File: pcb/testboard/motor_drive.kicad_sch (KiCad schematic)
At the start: 7 parts, among them IC1 TLE94112ESXUMA1, J3 Motor 1, J4 Motor 2, J5 Motor 3

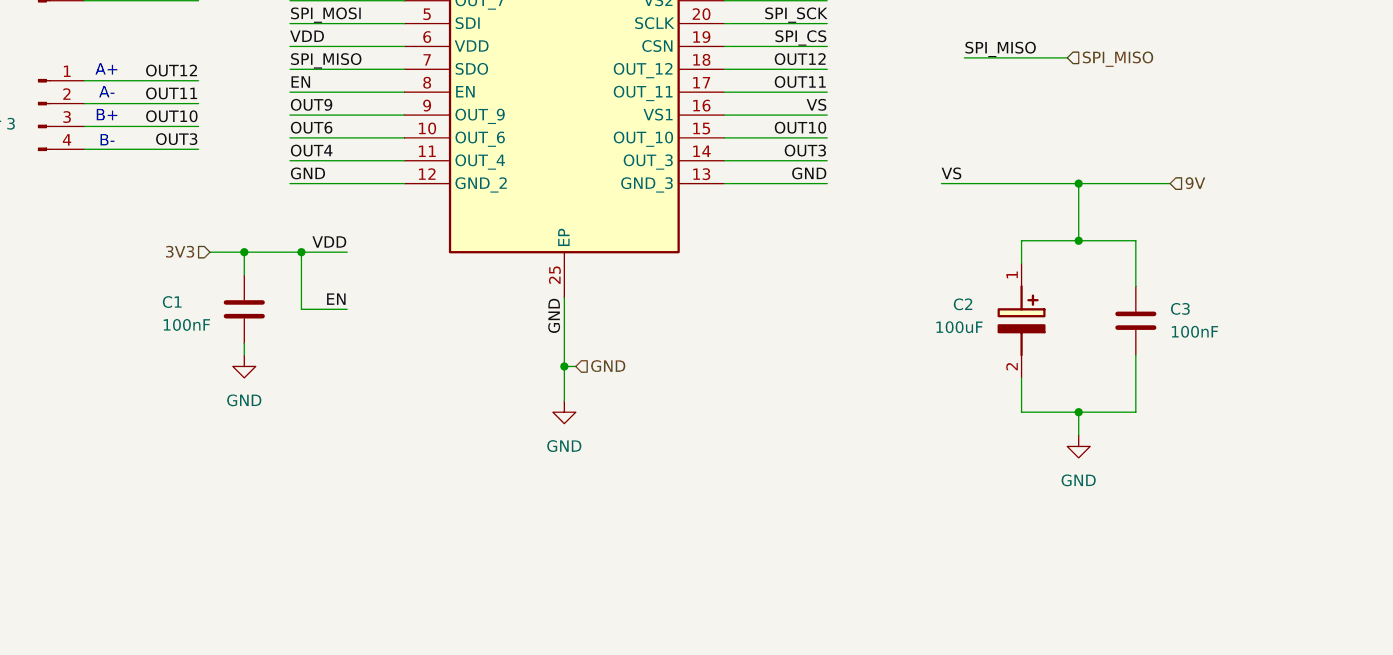
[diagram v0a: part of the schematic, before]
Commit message: Schematic final edit Added all remaining components and modifications, started PCB design
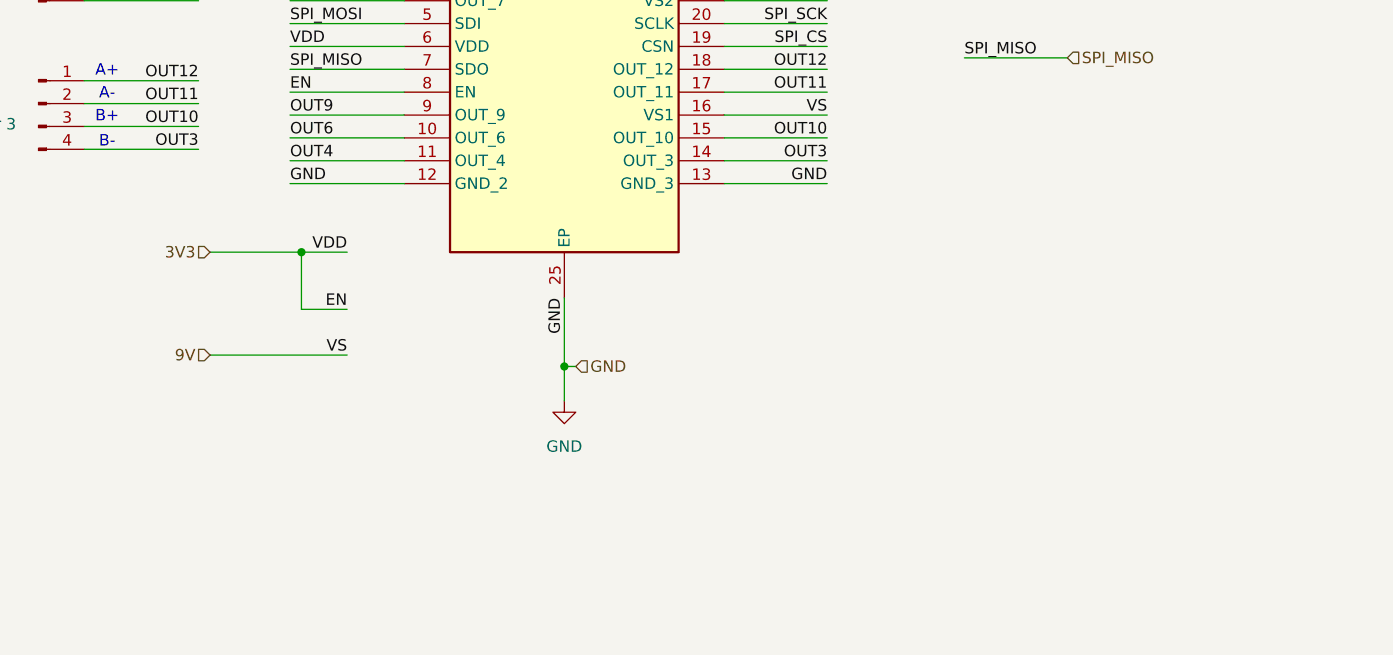
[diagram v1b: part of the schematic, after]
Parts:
- removed C1, C3: 100nF, Capacitor_SMD:C_0805_2012Metric, symbol Device:C
- removed C2: 100uF, CAPPRD250W50D655H1300, symbol EWH1EV101E11OT:EWH1EV101E11OT
- J3, J4, J5: footprint (none) -> Connector_PinSocket_1.00mm:PinSocket_1x04_P1.00mm_Vertical

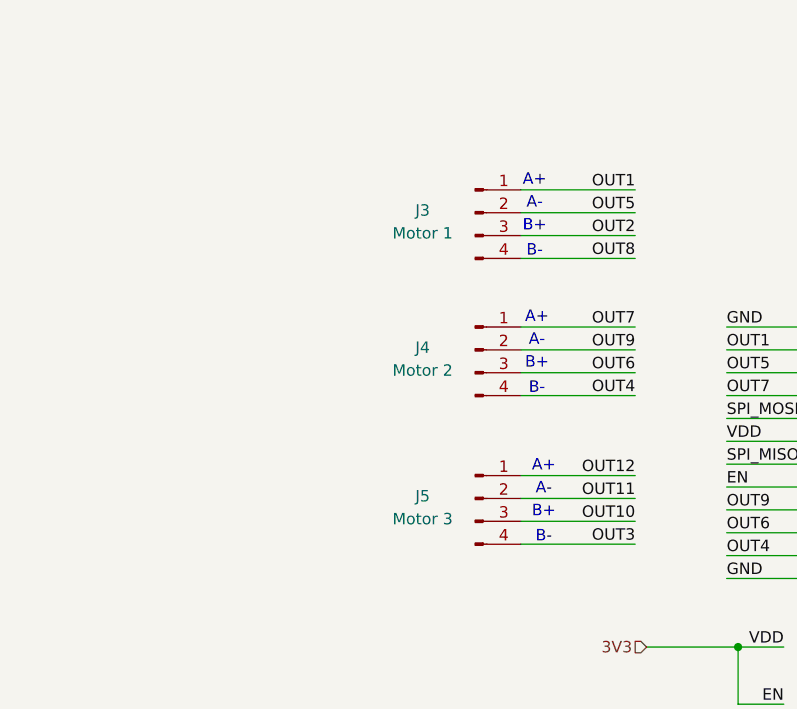
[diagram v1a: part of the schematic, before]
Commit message: routed the new connectors
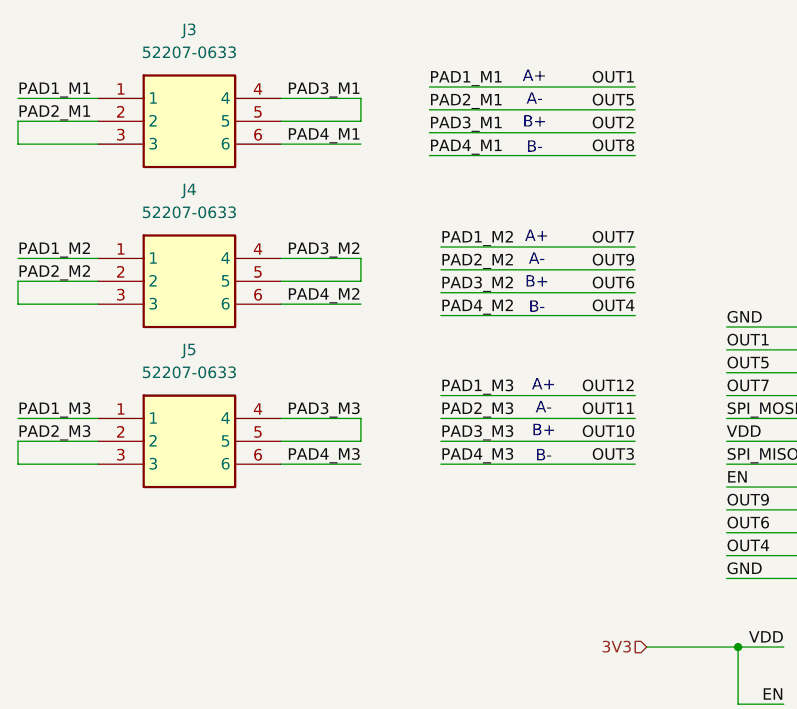
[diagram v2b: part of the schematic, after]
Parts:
- removed J3: Motor 1, Connector_PinSocket_1.00mm:PinSocket_1x04_P1.00mm_Vertical, symbol Connector:Conn_01x04_Pin
- removed J4: Motor 2, Connector_PinSocket_1.00mm:PinSocket_1x04_P1.00mm_Vertical, symbol Connector:Conn_01x04_Pin
- removed J5: Motor 3, Connector_PinSocket_1.00mm:PinSocket_1x04_P1.00mm_Vertical, symbol Connector:Conn_01x04_Pin
- added J3, J4, J5: 52207-0633, molex:52207-0633, symbol 52207-0633:52207-0633
- IC1: footprint SOP65P600X115-25N -> (none)
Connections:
- net OUT1: now also J3.1
- net OUT10: now also J5.4, J5.5
- net OUT11: now also J5.2, J5.3
- net OUT12: now also J5.1
- net OUT2: now also J3.4, J3.5
- net OUT3: now also J5.6
- net OUT4: now also J4.6
- net OUT5: now also J3.2, J3.3
- net OUT6: now also J4.4, J4.5
- net OUT7: now also J4.1
- net OUT8: now also J3.6
- net OUT9: now also J4.2, J4.3
